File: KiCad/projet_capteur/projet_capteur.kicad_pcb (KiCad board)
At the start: 2 copper layers, 68.6 x 53.3 mm, 9 parts, among them J1 Power, J2 Digital/PWM, J3 Analog, J4 Digital/PWM

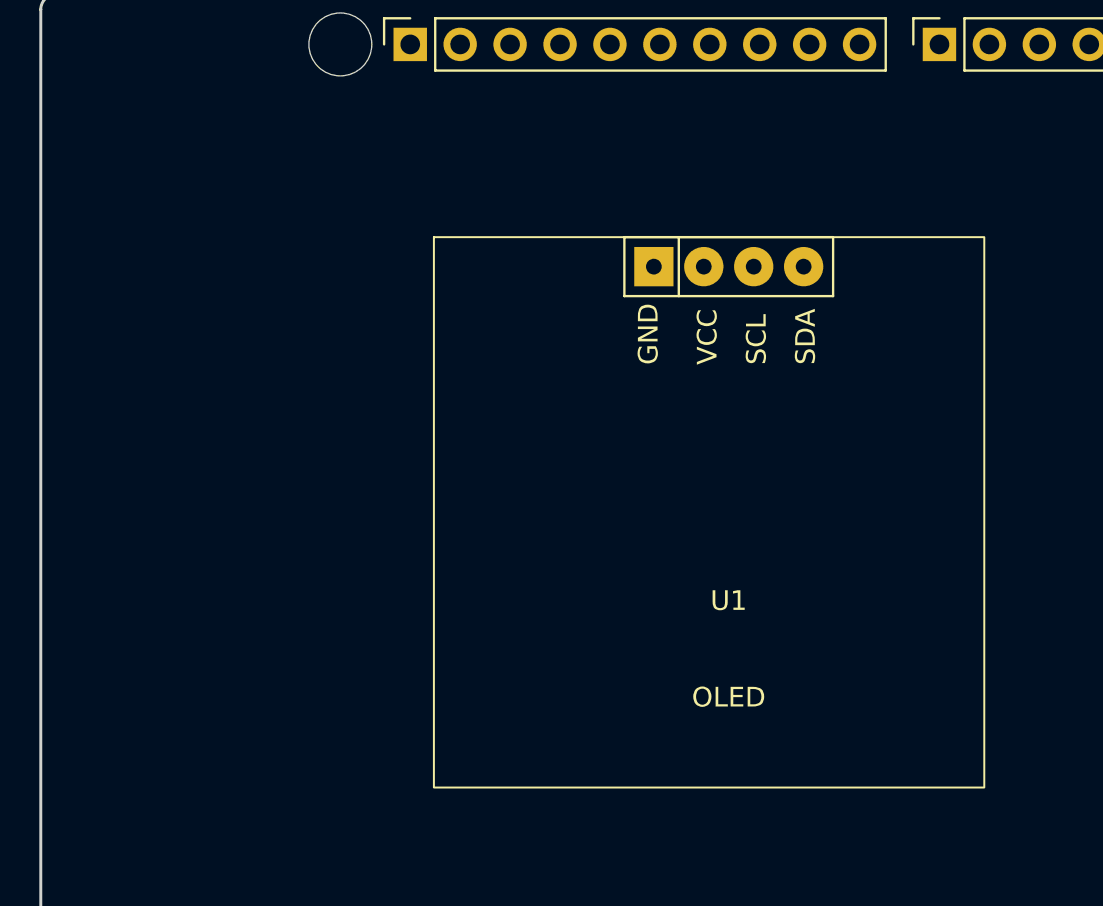
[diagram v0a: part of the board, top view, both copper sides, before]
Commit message: add 3D model to OLED
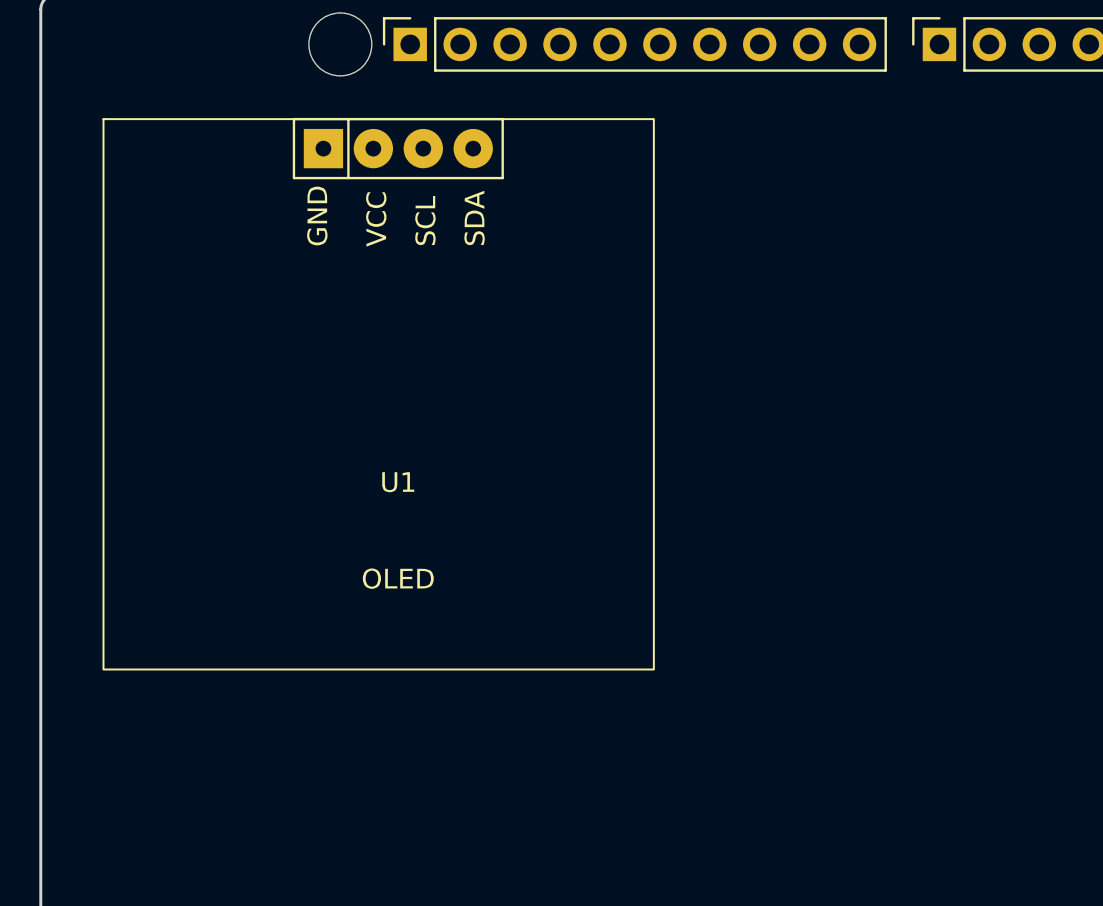
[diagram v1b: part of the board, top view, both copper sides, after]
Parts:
- moved U1 17.9 mm to (118.2, 54.5)
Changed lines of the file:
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@@
 (kicad_pcb
-	(version 20240108)
+	(version 20241229)
 	(generator "pcbnew")
-	(generator_version "8.0")
+	(generator_version "9.0")
 	(general
 		(thickness 1.6)
@@
 	(layers
 		(0 "F.Cu" signal)
-		(31 "B.Cu" signal)
-		(32 "B.Adhes" user "B.Adhesive")
-		(33 "F.Adhes" user "F.Adhesive")
-		(34 "B.Paste" user)
-		(35 "F.Paste" user)
-		(36 "B.SilkS" user "B.Silkscreen")
-		(37 "F.SilkS" user "F.Silkscreen")
-		(38 "B.Mask" user)
-		(39 "F.Mask" user)
-		(40 "Dwgs.User" user "User.Drawings")
-		(41 "Cmts.User" user "User.Comments")
-		(42 "Eco1.User" user "User.Eco1")
-		(43 "Eco2.User" user "User.Eco2")
-		(44 "Edge.Cuts" user)
-		(45 "Margin" user)
-		(46 "B.CrtYd" user "B.Courtyard")
-		(47 "F.CrtYd" user "F.Courtyard")
-		(48 "B.Fab" user)
-		(49 "F.Fab" user)
+		(2 "B.Cu" signal)
+		(9 "F.Adhes" user "F.Adhesive")
+		(11 "B.Adhes" user "B.Adhesive")
+		(13 "F.Paste" user)
+		(15 "B.Paste" user)
+		(5 "F.SilkS" user "F.Silkscreen")
+		(7 "B.SilkS" user "B.Silkscreen")
+		(1 "F.Mask" user)
+		(3 "B.Mask" user)
+		(17 "Dwgs.User" user "User.Drawings")
+		(19 "Cmts.User" user "User.Comments")
+		(21 "Eco1.User" user "User.Eco1")
+		(23 "Eco2.User" user "User.Eco2")
+		(25 "Edge.Cuts" user)
+		(27 "Margin" user)
+		(31 "F.CrtYd" user "F.Courtyard")
+		(29 "B.CrtYd" user "B.Courtyard")
+		(35 "F.Fab" user)
+		(33 "B.Fab" user)
 	)
 	(setup
@@
 		(pad_to_mask_clearance 0)
 		(allow_soldermask_bridges_in_footprints no)
+		(tenting front back)
 		(aux_axis_origin 100 100)
 		(grid_origin 100 100)
 		(pcbplotparams
-			(layerselection 0x0000030_80000001)
-			(plot_on_all_layers_selection 0x0000000_00000000)
+			(layerselection 0x00000000_00000000_00000000_000000a5)
+			(plot_on_all_layers_selection 0x00000000_00000000_00000000_00000000)
 			(disableapertmacros no)
 			(usegerberextensions no)
@@
 			(svgprecision 6)
 			(plotframeref no)
-			(viasonmask no)
 			(mode 1)
 			(useauxorigin no)
@@
 			(pdf_front_fp_property_popups yes)
 			(pdf_back_fp_property_popups yes)
+			(pdf_metadata yes)
+			(pdf_single_document no)
 			(dxfpolygonmode yes)
 			(dxfimperialunits yes)
@@
 			(psnegative no)
 			(psa4output no)
-			(plotreference yes)
-			(plotvalue yes)
-			(plotfptext yes)
+			(plot_black_and_white yes)
 			(plotinvisibletext no)
 			(sketchpadsonfab no)
+			(plotpadnumbers no)
+			(hidednponfab no)
+			(sketchdnponfab yes)
+			(crossoutdnponfab yes)
 			(subtractmaskfromsilk no)
 			(outputformat 1)
@@
 			)
 		)
-		(property "Footprint" "Connector_PinSocket_2.54mm:PinSocket_1x08_P2.54mm_Vertical"
-			(at 0 0 90)
-			(unlocked yes)
-			(layer "F.Fab")
-			(hide yes)
-			(effects
-				(font
-					(size 1.27 1.27)
-					(thickness 0.15)
-				)
-			)
-		)
 		(property "Datasheet" ""
 			(at 0 0 90)
@@
 		)
 		(property ki_fp_filters "Connector*:*_1x??_*")
-		(sheetname "Racine")
+		(sheetname "/")
 		(sheetfile "projet_capteur.kicad_sch")
 		(attr through_hole)
@@
 			(pintype "passive")
 		)
+		(embedded_fonts no)
 		(model "${KICAD7_3DMODEL_DIR}/Connector_PinSocket_2.54mm.3dshapes/PinSocket_1x08_P2.54mm_Vertical.wrl"
 			(offset
@@
 			)
 		)
-		(property "Footprint" "Connector_PinSocket_2.54mm:PinSocket_1x06_P2.54mm_Vertical"
-			(at 0 0 90)
-			(unlocked yes)
-			(layer "F.Fab")
-			(hide yes)
-			(effects
-				(font
-					(size 1.27 1.27)
-					(thickness 0.15)
-				)
-			)
-		)
 		(property "Datasheet" ""
 			(at 0 0 90)
@@
 		)
 		(property ki_fp_filters "Connector*:*_1x??_*")
-		(sheetname "Racine")
+		(sheetname "/")
 		(sheetfile "projet_capteur.kicad_sch")
 		(attr through_hole)
@@
 			(pintype "passive")
 		)
+		(embedded_fonts no)
 		(model "${KICAD7_3DMODEL_DIR}/Connector_PinSocket_2.54mm.3dshapes/PinSocket_1x06_P2.54mm_Vertical.wrl"
 			(offset
@@
 			)
 		)
-		(property "Footprint" "Connector_PinSocket_2.54mm:PinSocket_1x10_P2.54mm_Vertical"
-			(at 0 0 90)
-			(unlocked yes)
-			(layer "F.Fab")
-			(hide yes)
-			(effects
-				(font
-					(size 1.27 1.27)
-					(thickness 0.15)
-				)
-			)
-		)
 		(property "Datasheet" ""
 			(at 0 0 90)
@@
 		)
 		(property ki_fp_filters "Connector*:*_1x??_*")
-		(sheetname "Racine")
+		(sheetname "/")
 		(sheetfile "projet_capteur.kicad_sch")
 		(attr through_hole)
@@
 			(pintype "passive")
 		)
+		(embedded_fonts no)
 		(model "${KICAD7_3DMODEL_DIR}/Connector_PinSocket_2.54mm.3dshapes/PinSocket_1x10_P2.54mm_Vertical.wrl"
 			(offset
@@
 			)
 		)
-		(property "Footprint" "Connector_PinSocket_2.54mm:PinSocket_1x08_P2.54mm_Vertical"
-			(at 0 0 90)
-			(unlocked yes)
-			(layer "F.Fab")
-			(hide yes)
-			(effects
-				(font
-					(size 1.27 1.27)
-					(thickness 0.15)
-				)
-			)
-		)
 		(property "Datasheet" ""
 			(at 0 0 90)
@@
 		)
 		(property ki_fp_filters "Connector*:*_1x??_*")
-		(sheetname "Racine")
+		(sheetname "/")
 		(sheetfile "projet_capteur.kicad_sch")
 		(attr through_hole)
@@
 			(pintype "passive")
 		)
+		(embedded_fonts no)
 		(model "${KICAD7_3DMODEL_DIR}/Connector_PinSocket_2.54mm.3dshapes/PinSocket_1x08_P2.54mm_Vertical.wrl"
 			(offset
@@
 	(footprint "Lib_empreint:SIP-4"
 		(layer "F.Cu")
-		(at 135 60.505)
+		(at 118.19 54.5)
 		(property "Reference" "U1"
 			(at 0 17 0)
@@
 			)
 		)
-		(property "Footprint" "Lib_empreint:SIP-4"
-			(at 0 0 0)
-			(layer "F.Fab")
-			(hide yes)
-			(effects
-				(font
-					(size 1.27 1.27)
-					(thickness 0.15)
-				)
-			)
-		)
 		(property "Datasheet" ""
 			(at 0 0 0)
@@
 			)
 		)
-		(sheetname "Racine")
+		(sheetname "/")
 		(sheetfile "projet_capteur.kicad_sch")
 		(attr through_hole)
@@
 				(type default)
 			)
-			(fill none)
+			(fill no)
 			(layer "F.SilkS")
 		)
@@
 			(pinfunction "SDA")
 			(pintype "input")
+		)
+		(embedded_fonts no)
+		(model "C:/Github/2024-2025-4GP-Yoann-LyHai-VietHoang/KiCad/Model_3D/pantalla-oled-0-96-128x64-1.snapshot.7/Pantalla OLED 0.96'' 128x64.stp"
+			(offset
+				(xyz -0.5 -12.2 3)
+			)
+			(scale
+				(xyz 1 1 1)
+			)
+			(rotate
+				(xyz -0 -0 -0)
+			)
 		)
 	)
@@
 			)
 		)
-		(property "Footprint" ""
-			(at 0 0 0)
-			(unlocked yes)
-			(layer "F.Fab")
-			(hide yes)
-			(effects
-				(font
-					(size 1.27 1.27)
-					(thickness 0.15)
-				)
-			)
-		)
 		(property "Datasheet" ""
 			(at 0 0 0)
@@
 				(type solid)
 			)
-			(fill none)
+			(fill no)
 			(layer "F.CrtYd")
 		)
@@
 			(layers "*.Cu" "*.Mask")
 		)
+		(embedded_fonts no)
 	)
 	(footprint "Arduino_MountingHole:MountingHole_3.2mm"
@@
 			)
 		)
-		(property "Footprint" ""
-			(at 0 0 0)
-			(unlocked yes)
-			(layer "F.Fab")
-			(hide yes)
-			(effects
-				(font
-					(size 1.27 1.27)
-					(thickness 0.15)
-				)
-			)
-		)
 		(property "Datasheet" ""
 			(at 0 0 0)
@@
 				(type solid)
 			)
-			(fill none)
+			(fill no)
 			(layer "F.CrtYd")
 		)
@@
 			(layers "*.Cu" "*.Mask")
 		)
+		(embedded_fonts no)
 	)
 	(footprint "Arduino_MountingHole:MountingHole_3.2mm"
@@
 			)
 		)
-		(property "Footprint" ""
-			(at 0 0 0)
-			(unlocked yes)
-			(layer "F.Fab")
-			(hide yes)
-			(effects
-				(font
-					(size 1.27 1.27)
-					(thickness 0.15)
-				)
-			)
-		)
 		(property "Datasheet" ""
 			(at 0 0 0)
@@
 				(type solid)
 			)
-			(fill none)
+			(fill no)
 			(layer "F.CrtYd")
 		)
@@
 			(layers "*.Cu" "*.Mask")
 		)
+		(embedded_fonts no)
 	)
 	(footprint "Arduino_MountingHole:MountingHole_3.2mm"
@@
 			)
 		)
-		(property "Footprint" ""
-			(at 0 0 0)
-			(unlocked yes)
-			(layer "F.Fab")
-			(hide yes)
-			(effects
-				(font
-					(size 1.27 1.27)
-					(thickness 0.15)
-				)
-			)
-		)
 		(property "Datasheet" ""
 			(at 0 0 0)
@@
 				(type solid)
 			)
-			(fill none)
+			(fill no)
 			(layer "F.CrtYd")
 		)
@@
 			(layers "*.Cu" "*.Mask")
 		)
+		(embedded_fonts no)
 	)
 	(gr_line
@@
 			(type solid)
 		)
-		(fill none)
+		(fill no)
 		(layer "Dwgs.User")
 	)
@@
 		)
 	)
+	(embedded_fonts no)
 )

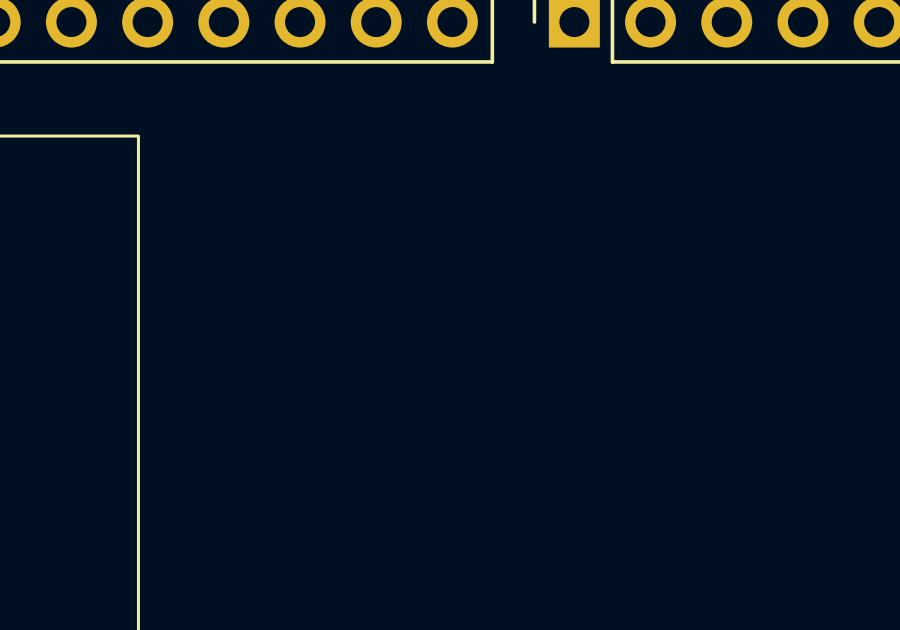
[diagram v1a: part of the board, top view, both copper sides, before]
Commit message: Ajout FlexSensor
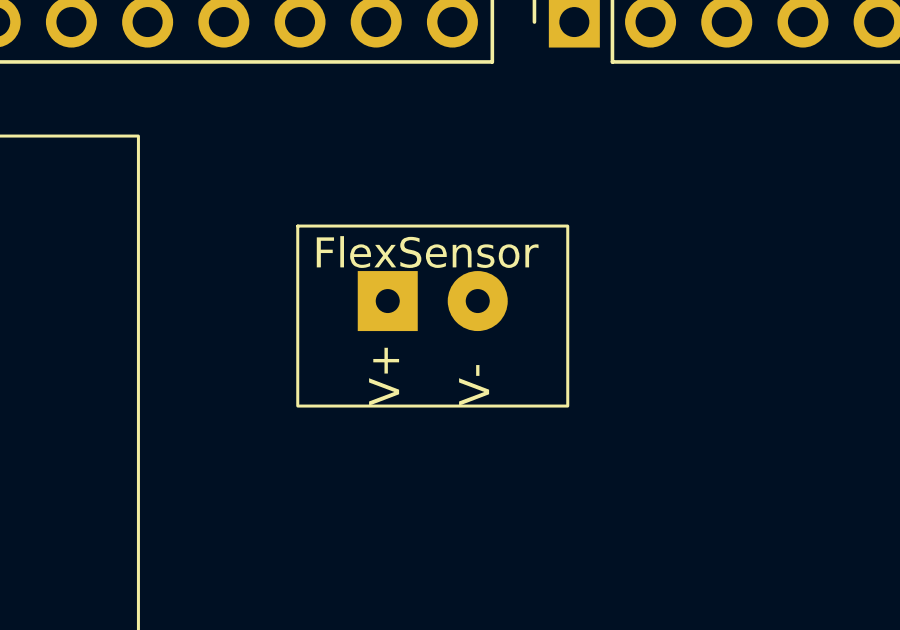
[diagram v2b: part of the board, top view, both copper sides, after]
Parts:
- added U2: ~, Lib_empreint:Empreinte_FlexSensor, F.Cu at (144.0, 58.5)
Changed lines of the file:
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@@
 	(net 31 "unconnected-(U1-SDA-Pad4)")
 	(net 32 "unconnected-(U1-GND-Pad1)")
+	(net 33 "unconnected-(U2-V--Pad2)")
+	(net 34 "unconnected-(U2-V+-Pad1)")
 	(footprint "Connector_PinSocket_2.54mm:PinSocket_1x08_P2.54mm_Vertical"
 		(locked yes)
@@
 		)
 		(embedded_fonts no)
+	)
+	(footprint "Lib_empreint:Empreinte_FlexSensor"
+		(layer "F.Cu")
+		(at 144 58.5)
+		(property "Reference" "U2"
+			(at -1 -0.5 0)
+			(unlocked yes)
+			(layer "F.SilkS")
+			(hide yes)
+			(effects
+				(font
+					(size 1 1)
+					(thickness 0.1)
+				)
+			)
+		)
+		(property "Value" "~"
+			(at 0 1 0)
+			(unlocked yes)
+			(layer "F.Fab")
+			(hide yes)
+			(effects
+				(font
+					(size 1 1)
+					(thickness 0.15)
+				)
+			)
+		)
+		(property "Datasheet" ""
+			(at 0 0 0)
+			(unlocked yes)
+			(layer "F.Fab")
+			(hide yes)
+			(effects
+				(font
+					(size 1 1)
+					(thickness 0.15)
+				)
+			)
+		)
+		(property "Description" ""
+			(at 0 0 0)
+			(unlocked yes)
+			(layer "F.Fab")
+			(hide yes)
+			(effects
+				(font
+					(size 1 1)
+					(thickness 0.15)
+				)
+			)
+		)
+		(sheetname "/")
+		(sheetfile "projet_capteur.kicad_sch")
+		(attr smd)
+		(fp_rect
+			(start -7.5 -2.5)
+			(end 1.5 3.5)
+			(stroke
+				(width 0.1)
+				(type default)
+			)
+			(fill no)
+			(layer "F.SilkS")
+		)
+		(fp_text user "V+"
+			(at -4 3.5 90)
+			(unlocked yes)
+			(layer "F.SilkS")
+			(effects
+				(font
+					(size 1 1)
+					(thickness 0.1)
+				)
+				(justify left bottom)
+			)
+		)
+		(fp_text user "FlexSensor"
+			(at -7 -1 0)
+			(unlocked yes)
+			(layer "F.SilkS")
+			(effects
+				(font
+					(size 1 1)
+					(thickness 0.1)
+				)
+				(justify left bottom)
+			)
+		)
+		(fp_text user "V-"
+			(at -1 3.5 90)
+			(unlocked yes)
+			(layer "F.SilkS")
+			(effects
+				(font
+					(size 1 1)
+					(thickness 0.1)
+				)
+				(justify left bottom)
+			)
+		)
+		(pad "1" thru_hole rect
+			(at -4.5 0)
+			(size 2 2)
+			(drill 0.8)
+			(layers "*.Cu" "*.Mask")
+			(remove_unused_layers no)
+			(net 34 "unconnected-(U2-V+-Pad1)")
+			(pinfunction "V+")
+			(pintype "input")
+			(thermal_bridge_angle 45)
+		)
+		(pad "2" thru_hole circle
+			(at -1.5 0)
+			(size 2 2)
+			(drill 0.8)
+			(layers "*.Cu" "*.Mask")
+			(remove_unused_layers no)
+			(net 33 "unconnected-(U2-V--Pad2)")
+			(pinfunction "V-")
+			(pintype "output")
+		)
+		(embedded_fonts no)

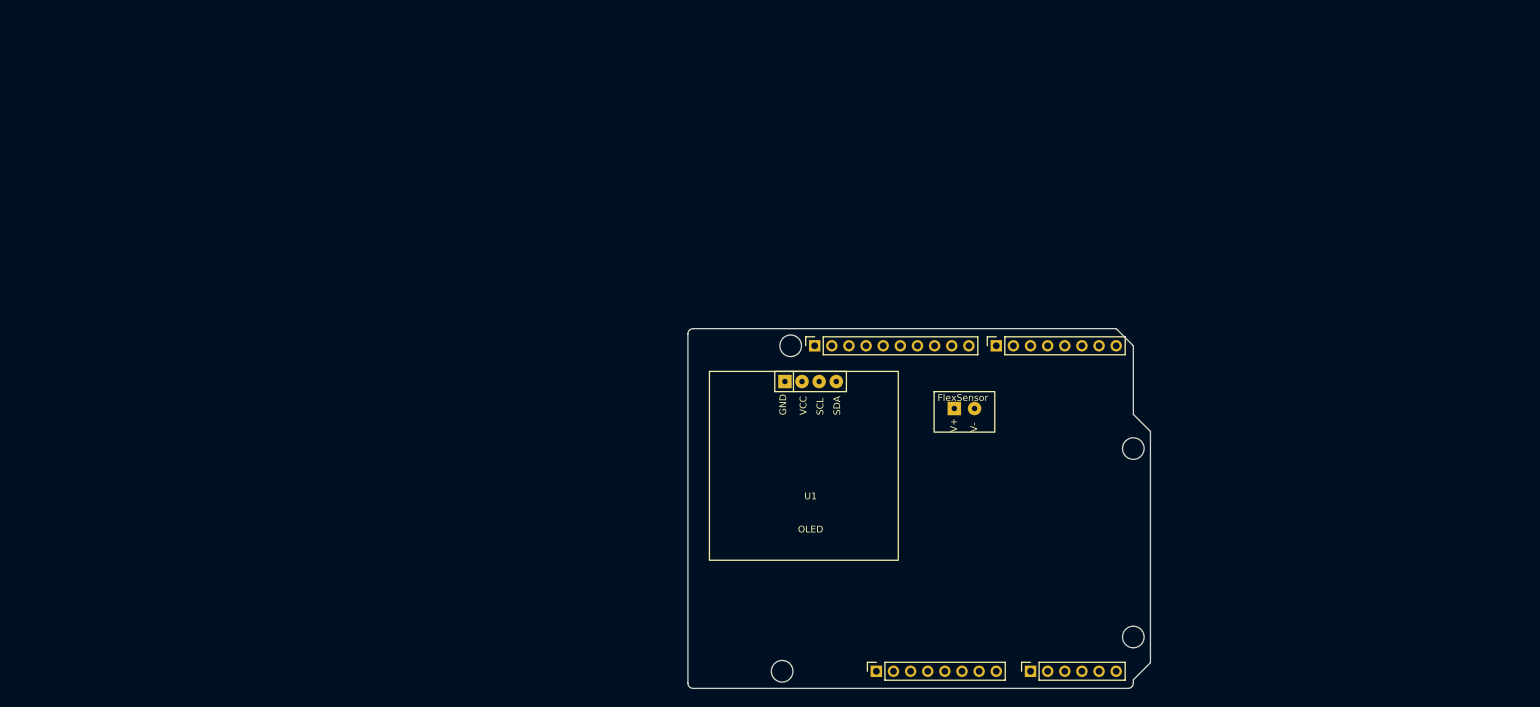
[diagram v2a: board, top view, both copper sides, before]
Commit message: Add empreintes into PCB
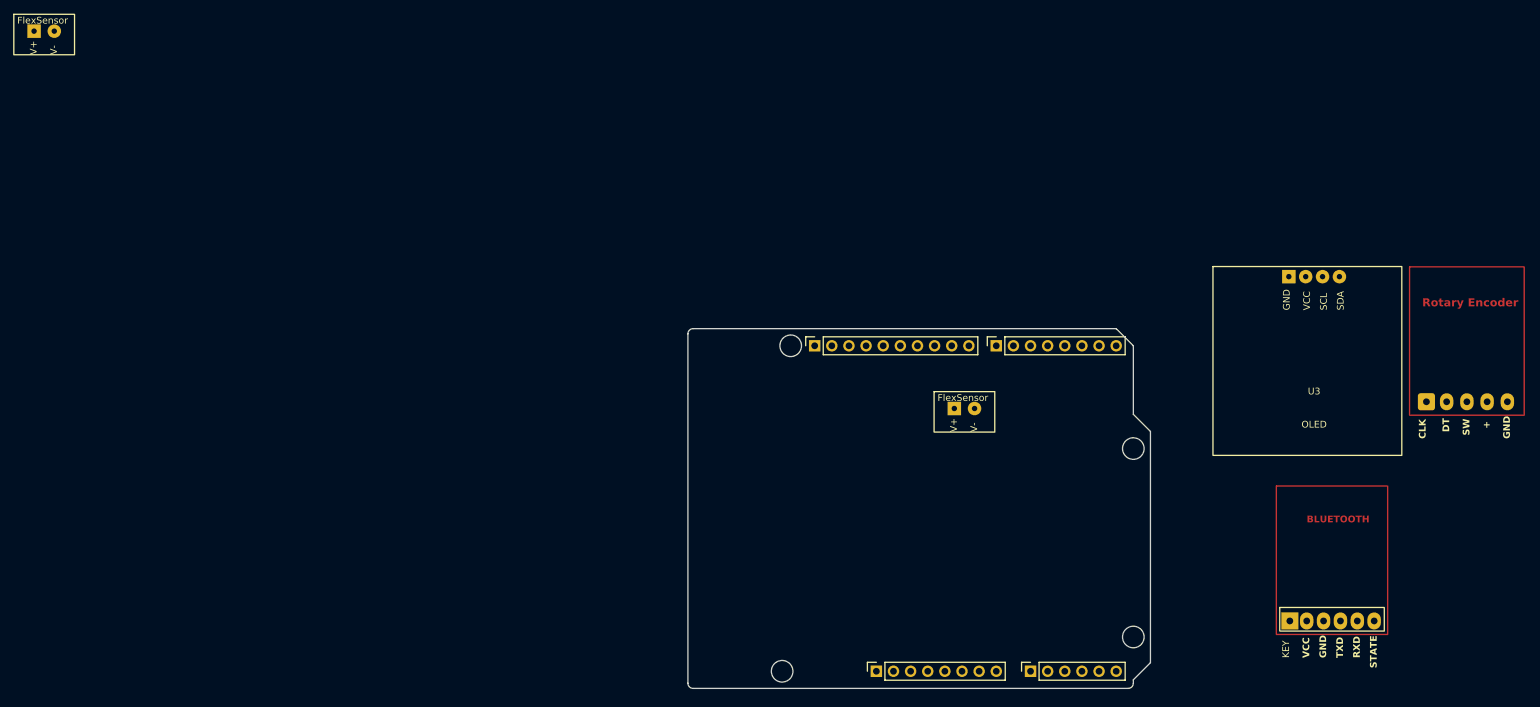
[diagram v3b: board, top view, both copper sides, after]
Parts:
- added U2: ~, Lib_empreint:Empreinte_Rotary_Encoder, F.Cu at (209.5, 57.5)
- added U3: ~, Lib_empreint:Empreinte_OLED, F.Cu at (192.8, 39.0)
- added U4: ~, Lib_empreint:Empreinte_FlexSensor, F.Cu at (7.55, 2.55)
- U1: footprint Lib_empreint:SIP-4 -> Lib_empreint:Empreinte_Bluetooth
- moved U1 79.4 mm to (189.2, 90.0)
